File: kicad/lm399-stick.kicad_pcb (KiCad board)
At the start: 4 copper layers, 48.3 x 48.3 mm, 14 parts, among them P1 CONN_5X1, U1 LM399A, U2 OP07

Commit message: v1
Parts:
- removed the G*** at (59.7, 54.0)
- removed the H*** at (167.6, 133.3)
- removed the H*** at (208.3, 133.3)
- removed the H*** at (208.3, 174.0)
- removed the H*** at (167.6, 174.0)
- added C4: 10nF, ANYSSCAP_SMALL_2_059B_0805, F.Cu at (165.1, 143.5)
- added G***: OSHW-logo_silkscreen-front_3mm, OSHW-logo_silkscreen-front_3mm, F.Cu at (196.2, 139.1)
- added H***: VAL**, SIL-1, F.Cu at (209.6, 137.2)
- added H***: VAL**, SIL-1, F.Cu at (209.6, 149.9)
- added P2: CONN_1X1, SIL-1, F.Cu at (165.1, 137.2)
- added P3: CONN_1X1, SIL-1, F.Cu at (188.0, 144.8)
- added P4: CONN_1X1, SIL-1, F.Cu at (188.0, 142.2)
- added P5: CONN_2X1, SIL-2, F.Cu at (182.9, 149.9)
- added R4: 200k, R_AXIAL_0W25_059A_PL, F.Cu at (185.4, 147.3)
- C1, C2, C3: footprint CERCAP_2_059A -> ANYSSCAP_SMALL_2_059B_0805
- P1: value CONN_5X1 -> CONN_1X1; footprint 4455-N2-5 -> SIL-1
- moved U1 28.4 mm to (203.8, 141.6), turned to 0 degrees
- moved P1 26.8 mm to (165.1, 149.9)
- moved R1 15.7 mm to (182.9, 137.2)
- moved C1 10.6 mm to (191.1, 143.5)
- moved R2 10.5 mm to (167.6, 138.4)
- moved U2 6.35 mm to (180.3, 144.8), turned to 90 degrees
- moved R3 5.68 mm to (170.2, 148.6)
- moved C2 5.39 mm to (191.8, 149.9), turned to 0 degrees
- moved C3 5.39 mm to (176.5, 149.9), turned to 0 degrees
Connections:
- C1 pad 1: +Vref -> +Vz
- C1 pad 2: -Vref -> -Vz
- C2 pad 1: 15V -> N-000002
- C2 pad 2: -Vref -> -Vz
- C3 pad 1: N-000006 -> Vcc
- C3 pad 2: N-000007 -> -Vz
- P1 pad 1: 15V -> Vcc
- R1 pad 1: N-000006 -> N-000004
- R1 pad 2: +Vref -> +Vz
- R2 pad 1: N-000006 -> N-000004
- R3 pad 2: -Vref -> -Vz
- U1 pad 1: +Vref -> +Vz
- U1 pad 2: -Vref -> -Vz
- U1 pad 3: 15V -> N-000002
- U1 pad 4: -Vref -> -Vz
- U2 pad 3: +Vref -> +Vz
- U2 pad 4: -Vref -> -Vz
- U2 pad 6: N-000006 -> N-000004
- U2 pad 7: 15V -> Vcc
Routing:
- net -Vref: track 160.4 -> 0.00 mm
- net -Vz: track 0.00 -> 131.7 mm
- net 15V: track 77.4 -> 0.00 mm
- net +Vref: track 70.2 -> 0.00 mm
- net +Vz: track 0.00 -> 63.8 mm
- net Vcc: track 0.00 -> 31.1 mm
- net N-000006: track 25.0 -> 0.00 mm
- net N-000002: track 0.00 -> 23.7 mm
- net N-000004: track 0.00 -> 20.4 mm
- net N-000007: track 15.5 -> 23.7 mm
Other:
- board size 48.3 x 48.3 mm -> 48.3 x 16.5 mm
- board text added: "+Vz"
- board text added: "-Vz"
- board text added: "GND"
- board text added: "LM399 on a stick!"
- board text added: "VCC"
- board text added: "github.com/pepaslabs/lm399-stick"
- board text removed: "Small LM399"
- board text removed: "github.com/pepaslabs/small-lm399"

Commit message: correcting cap values
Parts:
- C3: value 10nF -> 0.1uF
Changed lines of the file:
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@@
     (links 25)
     (no_connects 0)
-    (area 145.999999 116.789999 237.540001 190.550001)
+    (area 161.383134 133.9088 211.996866 153.1112)
     (thickness 1.6)
     (drawings 31)
@@
       (effects (font (size 0.635 0.635) (thickness 0.127)))
     )
-    (fp_text value 10nF (at 2.54 -1.905) (layer F.SilkS)
-      (effects (font (size 0.635 0.635) (thickness 0.127)))
-    )
+    (fp_text value 0.1uF (at 2.54 -1.905) (layer F.SilkS)
+      (effects (font (size 0.635 0.635) (thickness 0.127)))
+    )

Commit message: v1.1
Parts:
- removed the H*** at (209.6, 137.2)
- removed the H*** at (209.6, 149.9)
- added H***: Val**, 1pin_056_079, F.Cu at (209.6, 149.9)
- added H***: Val**, 1pin_056_079, F.Cu at (209.6, 137.2)
- P1, P2, P3, P4: footprint SIL-1 -> 1pin_056_079
- moved P4 0.64 mm to (188.0, 141.6)
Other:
- board text added: "v1.1"
- board text removed: "v1"
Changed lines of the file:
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@@
     (links 25)
     (no_connects 0)
-    (area 161.383134 133.9088 211.996866 153.1112)
+    (area 163.144999 135.204999 211.505001 151.815001)
     (thickness 1.6)
     (drawings 31)
@@
     (mod_text_size 1 1)
     (mod_text_width 0.15)
-    (pad_size 0.8128 0.8128)
-    (pad_drill 0.4064)
+    (pad_size 2.0066 2.0066)
+    (pad_drill 1.4224)
     (pad_to_mask_clearance 0)
     (aux_axis_origin 0 0)
@@
     )
   )
-  (module SIL-1 (layer F.Cu)
-    (at 165.1 149.86)
-    (descr "Connecteurs 1 pin")
-    (tags "CONN DEV")
-    (fp_text reference P1 (at 0 2.54) (layer F.SilkS) hide
-      (effects (font (size 0.762 0.762) (thickness 0.1524)))
-    )
-    (fp_text value CONN_1X1 (at 0 -2.54) (layer F.SilkS) hide
-      (effects (font (size 0.762 0.762) (thickness 0.1524)))
-    )
-    (fp_line (start -1.27 1.27) (end 1.27 1.27) (layer F.SilkS) (width 0.254))
-    (fp_line (start -1.27 -1.27) (end 1.27 -1.27) (layer F.SilkS) (width 0.254))
-    (fp_line (start -1.27 1.27) (end -1.27 -1.27) (layer F.SilkS) (width 0.254))
-    (fp_line (start 1.27 -1.27) (end 1.27 1.27) (layer F.SilkS) (width 0.254))
-    (pad 1 thru_hole rect (at 0 0) (size 1.7526 1.7526) (drill 1.016)
-      (layers *.Cu *.Mask F.SilkS)
-      (net 6 Vcc)
-    )
-  )
-  (module SIL-1 (layer F.Cu)
-    (at 165.1 137.16)
-    (descr "Connecteurs 1 pin")
-    (tags "CONN DEV")
-    (fp_text reference P2 (at 0 2.54) (layer F.SilkS) hide
-      (effects (font (size 0.762 0.762) (thickness 0.1524)))
-    )
-    (fp_text value CONN_1X1 (at 0 -2.54) (layer F.SilkS) hide
-      (effects (font (size 0.762 0.762) (thickness 0.1524)))
-    )
-    (fp_line (start -1.27 1.27) (end 1.27 1.27) (layer F.SilkS) (width 0.254))
-    (fp_line (start -1.27 -1.27) (end 1.27 -1.27) (layer F.SilkS) (width 0.254))
-    (fp_line (start -1.27 1.27) (end -1.27 -1.27) (layer F.SilkS) (width 0.254))
-    (fp_line (start 1.27 -1.27) (end 1.27 1.27) (layer F.SilkS) (width 0.254))
-    (pad 1 thru_hole rect (at 0 0) (size 1.7526 1.7526) (drill 1.016)
-      (layers *.Cu *.Mask F.SilkS)
-      (net 2 -Vz)
-    )
-  )
-  (module SIL-1 (layer F.Cu)
-    (at 187.96 144.78)
-    (descr "Connecteurs 1 pin")
-    (tags "CONN DEV")
-    (fp_text reference P3 (at 0 2.54) (layer F.SilkS) hide
-      (effects (font (size 0.762 0.762) (thickness 0.1524)))
-    )
-    (fp_text value CONN_1X1 (at 0 -2.54) (layer F.SilkS) hide
-      (effects (font (size 0.762 0.762) (thickness 0.1524)))
-    )
-    (fp_line (start -1.27 1.27) (end 1.27 1.27) (layer F.SilkS) (width 0.254))
-    (fp_line (start -1.27 -1.27) (end 1.27 -1.27) (layer F.SilkS) (width 0.254))
-    (fp_line (start -1.27 1.27) (end -1.27 -1.27) (layer F.SilkS) (width 0.254))
-    (fp_line (start 1.27 -1.27) (end 1.27 1.27) (layer F.SilkS) (width 0.254))
-    (pad 1 thru_hole rect (at 0 0) (size 1.7526 1.7526) (drill 1.016)
-      (layers *.Cu *.Mask F.SilkS)
-      (net 1 +Vz)
-    )
-  )
-  (module SIL-1 (layer F.Cu)
-    (at 187.96 142.24)
-    (descr "Connecteurs 1 pin")
-    (tags "CONN DEV")
-    (fp_text reference P4 (at 0 2.54) (layer F.SilkS) hide
-      (effects (font (size 0.762 0.762) (thickness 0.1524)))
-    )
-    (fp_text value CONN_1X1 (at 0 -2.54) (layer F.SilkS) hide
-      (effects (font (size 0.762 0.762) (thickness 0.1524)))
-    )
-    (fp_line (start -1.27 1.27) (end 1.27 1.27) (layer F.SilkS) (width 0.254))
-    (fp_line (start -1.27 -1.27) (end 1.27 -1.27) (layer F.SilkS) (width 0.254))
-    (fp_line (start -1.27 1.27) (end -1.27 -1.27) (layer F.SilkS) (width 0.254))
-    (fp_line (start 1.27 -1.27) (end 1.27 1.27) (layer F.SilkS) (width 0.254))
-    (pad 1 thru_hole rect (at 0 0) (size 1.7526 1.7526) (drill 1.016)
-      (layers *.Cu *.Mask F.SilkS)
-      (net 2 -Vz)
-    )
-  )
   (module R_AXIAL_0W25_059A_PL (layer F.Cu)
     (at 167.64 138.43 270)
@@
       (layers *.Cu *.Mask F.SilkS)
       (net 3 N-000002)
-    )
-  )
-  (module SIL-1 (layer F.Cu)
-    (at 209.55 137.16)
-    (descr "Connecteurs 1 pin")
-    (tags "CONN DEV")
-    (fp_text reference H*** (at 0 2.54) (layer F.SilkS) hide
-      (effects (font (size 0.762 0.762) (thickness 0.1524)))
-    )
-    (fp_text value VAL** (at 0 -2.54) (layer F.SilkS) hide
-      (effects (font (size 0.762 0.762) (thickness 0.1524)))
-    )
-    (fp_line (start -1.27 1.27) (end 1.27 1.27) (layer F.SilkS) (width 0.254))
-    (fp_line (start -1.27 -1.27) (end 1.27 -1.27) (layer F.SilkS) (width 0.254))
-    (fp_line (start -1.27 1.27) (end -1.27 -1.27) (layer F.SilkS) (width 0.254))
-    (fp_line (start 1.27 -1.27) (end 1.27 1.27) (layer F.SilkS) (width 0.254))
-    (pad 1 thru_hole rect (at 0 0) (size 1.7526 1.7526) (drill 1.016)
-      (layers *.Cu *.Mask F.SilkS)
-    )
-  )
-  (module SIL-1 (layer F.Cu)
-    (at 209.55 149.86)
-    (descr "Connecteurs 1 pin")
-    (tags "CONN DEV")
-    (fp_text reference H*** (at 0 2.54) (layer F.SilkS) hide
-      (effects (font (size 0.762 0.762) (thickness 0.1524)))
-    )
-    (fp_text value VAL** (at 0 -2.54) (layer F.SilkS) hide
-      (effects (font (size 0.762 0.762) (thickness 0.1524)))
-    )
-    (fp_line (start -1.27 1.27) (end 1.27 1.27) (layer F.SilkS) (width 0.254))
-    (fp_line (start -1.27 -1.27) (end 1.27 -1.27) (layer F.SilkS) (width 0.254))
-    (fp_line (start -1.27 1.27) (end -1.27 -1.27) (layer F.SilkS) (width 0.254))
-    (fp_line (start 1.27 -1.27) (end 1.27 1.27) (layer F.SilkS) (width 0.254))
-    (pad 1 thru_hole rect (at 0 0) (size 1.7526 1.7526) (drill 1.016)
-      (layers *.Cu *.Mask F.SilkS)
     )
   )
@@
       (xy -0.90932 1.3462)) (layer F.SilkS) (width 0.00254))
   )
+  (module 1pin_056_079 (layer F.Cu)
+    (at 165.1 137.16)
+    (descr "1 pin, 0.056\" drill, 0.079\" round pad")
+    (fp_text reference P2 (at 0 -2.54) (layer F.SilkS) hide
+      (effects (font (size 1.016 1.016) (thickness 0.254)))
+    )
+    (fp_text value CONN_1X1 (at 0 2.54) (layer F.SilkS) hide
+      (effects (font (size 1.016 1.016) (thickness 0.254)))
+    )
+    (pad 1 thru_hole circle (at 0 0) (size 2.0066 2.0066) (drill 1.4224)
+      (layers *.Cu *.Mask F.SilkS)
+      (net 2 -Vz)
+    )
+  )
+  (module 1pin_056_079 (layer F.Cu)
+    (at 165.1 149.86)
+    (descr "1 pin, 0.056\" drill, 0.079\" round pad")
+    (fp_text reference P1 (at 0 -2.54) (layer F.SilkS) hide
+      (effects (font (size 1.016 1.016) (thickness 0.254)))
+    )
+    (fp_text value CONN_1X1 (at 0 2.54) (layer F.SilkS) hide
+      (effects (font (size 1.016 1.016) (thickness 0.254)))
+    )
+    (pad 1 thru_hole rect (at 0 0) (size 2.0066 2.0066) (drill 1.4224)
+      (layers *.Cu *.Mask F.SilkS)
+      (net 6 Vcc)
+    )
+  )
+  (module 1pin_056_079 (layer F.Cu)
+    (at 209.55 149.86)
+    (descr "1 pin, 0.056\" drill, 0.079\" round pad")
+    (path 1pin)
+    (fp_text reference H*** (at 0 -2.54) (layer F.SilkS) hide
+      (effects (font (size 1.016 1.016) (thickness 0.254)))
+    )
+    (fp_text value Val** (at 0 2.54) (layer F.SilkS) hide
+      (effects (font (size 1.016 1.016) (thickness 0.254)))
+    )
+    (pad 1 thru_hole circle (at 0 0) (size 2.0066 2.0066) (drill 1.4224)
+      (layers *.Cu *.Mask F.SilkS)
+    )
+  )
+  (module 1pin_056_079 (layer F.Cu)
+    (at 209.55 137.16)
+    (descr "1 pin, 0.056\" drill, 0.079\" round pad")
+    (path 1pin)
+    (fp_text reference H*** (at 0 -2.54) (layer F.SilkS) hide
+      (effects (font (size 1.016 1.016) (thickness 0.254)))
+    )
+    (fp_text value Val** (at 0 2.54) (layer F.SilkS) hide
+      (effects (font (size 1.016 1.016) (thickness 0.254)))
+    )
+    (pad 1 thru_hole circle (at 0 0) (size 2.0066 2.0066) (drill 1.4224)
+      (layers *.Cu *.Mask F.SilkS)
+    )
+  )
+  (module 1pin_056_079 (layer F.Cu)
+    (at 187.96 141.605)
+    (descr "1 pin, 0.056\" drill, 0.079\" round pad")
+    (fp_text reference P4 (at 0 -2.54) (layer F.SilkS) hide
+      (effects (font (size 1.016 1.016) (thickness 0.254)))
+    )
+    (fp_text value CONN_1X1 (at 0 2.54) (layer F.SilkS) hide
+      (effects (font (size 1.016 1.016) (thickness 0.254)))
+    )
+    (pad 1 thru_hole circle (at 0 0) (size 2.0066 2.0066) (drill 1.4224)
+      (layers *.Cu *.Mask F.SilkS)
+      (net 2 -Vz)
+    )
+  )
+  (module 1pin_056_079 (layer F.Cu)
+    (at 187.96 144.78)
+    (descr "1 pin, 0.056\" drill, 0.079\" round pad")
+    (fp_text reference P3 (at 0 -2.54) (layer F.SilkS) hide
+      (effects (font (size 1.016 1.016) (thickness 0.254)))
+    )
+    (fp_text value CONN_1X1 (at 0 2.54) (layer F.SilkS) hide
+      (effects (font (size 1.016 1.016) (thickness 0.254)))
+    )
+    (pad 1 thru_hole rect (at 0 0) (size 2.0066 2.0066) (drill 1.4224)
+      (layers *.Cu *.Mask F.SilkS)
+      (net 1 +Vz)
+    )
+  )
   (gr_text +Vz (at 186.69 147.32) (layer F.SilkS)
     (effects (font (size 0.762 0.762) (thickness 0.1524)) (justify left))
@@
   (gr_arc (start 163.83 135.89) (end 163.195 135.89) (angle 90) (layer Edge.Cuts) (width 0.1))
   (gr_arc (start 163.83 151.13) (end 163.83 151.765) (angle 90) (layer Edge.Cuts) (width 0.1))
-  (gr_text v1 (at 199.39 136.525) (layer F.SilkS)
+  (gr_text v1.1 (at 199.39 136.525) (layer F.SilkS)
     (effects (font (size 0.635 0.635) (thickness 0.127)))
   )
@@
       )
     )
+  )
+  (zone (net 0) (net_name "") (layer B.SilkS) (hatch edge 0.508)
+    (connect_pads (clearance 0.508))
+    (min_thickness 0.254)
+    (fill (arc_segments 16) (thermal_gap 0.508) (thermal_bridge_width 0.508))
+    (polygon
+      (pts
+        (xy 179.07 148.59) (xy 173.99 148.59) (xy 173.99 135.89) (xy 179.07 135.89)
+      )
+    )

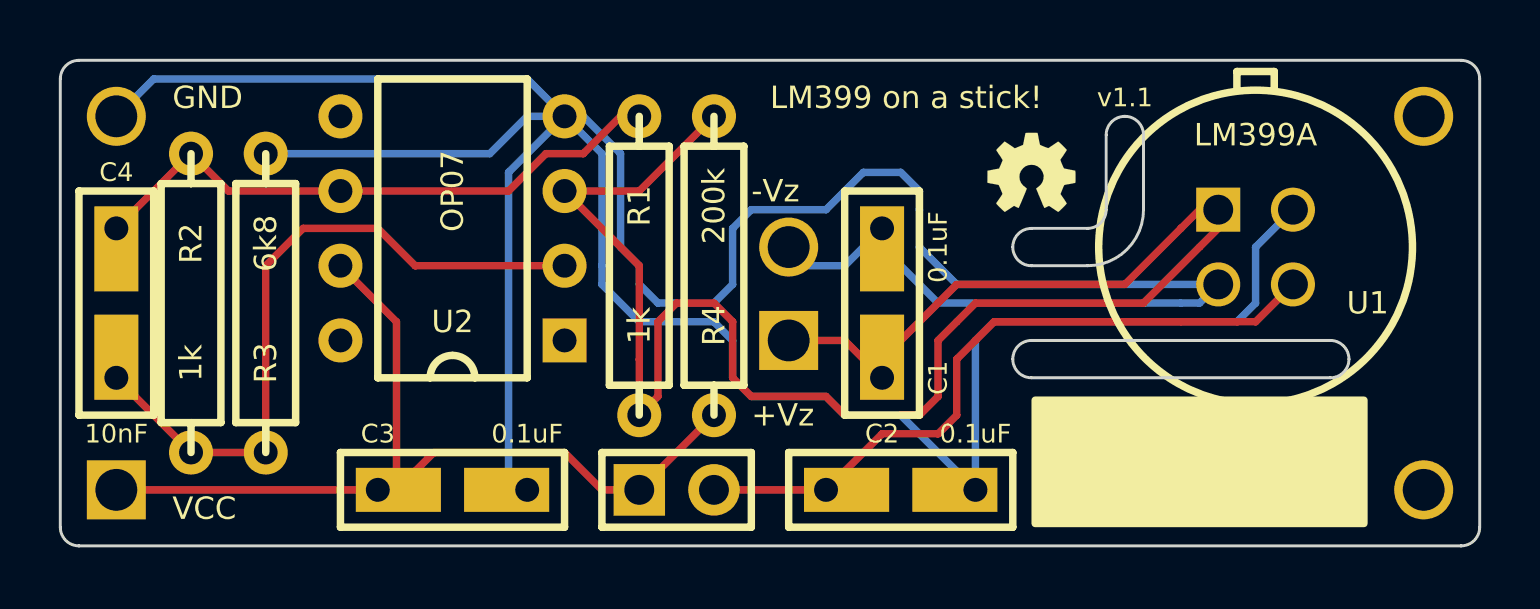
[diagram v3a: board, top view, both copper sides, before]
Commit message: using machine pin header footprints
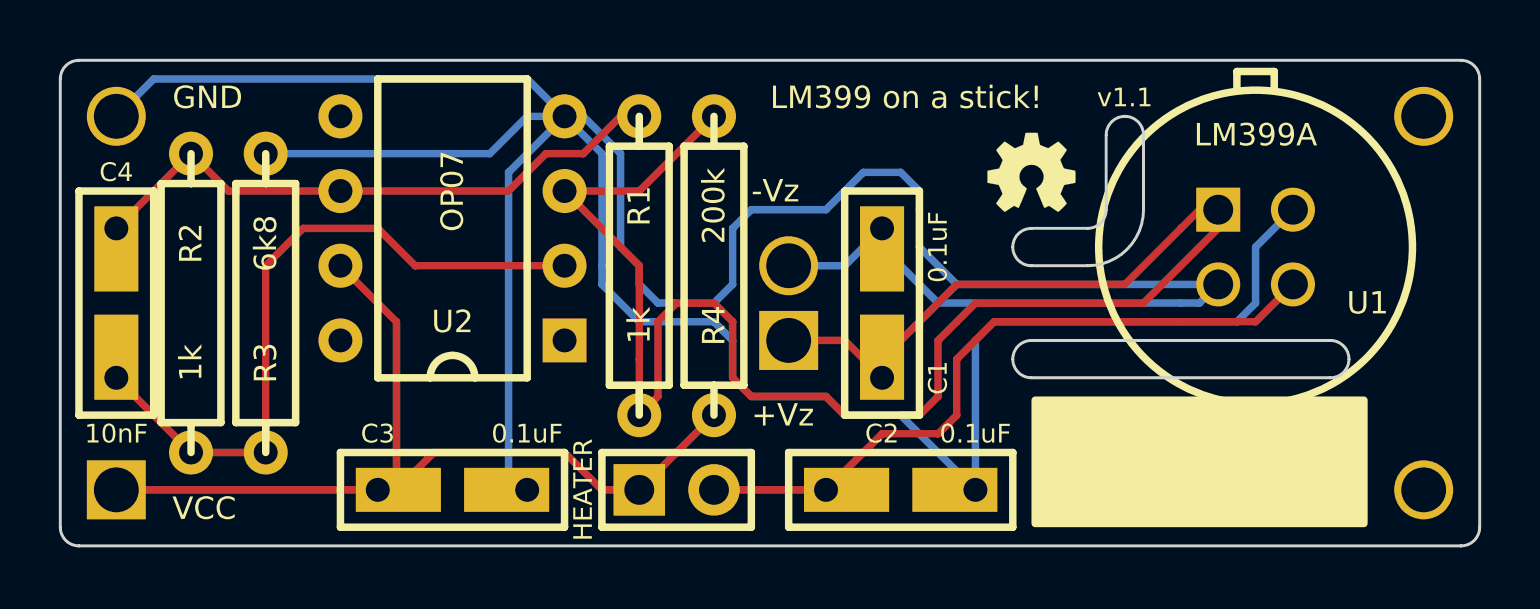
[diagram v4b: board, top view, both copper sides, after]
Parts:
- removed the H*** at (209.6, 149.9)
- removed the H*** at (209.6, 137.2)
- added H***: Val**, 1pin_060_079, F.Cu at (209.6, 137.2)
- added H***: Val**, 1pin_060_079, F.Cu at (209.6, 149.9)
- P1, P2, P3, P4: footprint 1pin_056_079 -> 1pin_060_079
- moved P4 0.64 mm to (188.0, 142.2)
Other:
- board text added: "HEATER"
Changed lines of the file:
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@@
     (links 25)
     (no_connects 0)
-    (area 163.144999 135.204999 211.505001 151.815001)
+    (area 160.203445 133.731 212.753222 153.289)
     (thickness 1.6)
-    (drawings 31)
+    (drawings 32)
     (tracks 124)
     (zones 0)
@@
     (mod_text_width 0.15)
     (pad_size 2.0066 2.0066)
-    (pad_drill 1.4224)
+    (pad_drill 1.524)
     (pad_to_mask_clearance 0)
     (aux_axis_origin 0 0)
@@
       (xy -0.90932 1.3462)) (layer F.SilkS) (width 0.00254))
   )
-  (module 1pin_056_079 (layer F.Cu)
-    (at 165.1 137.16)
-    (descr "1 pin, 0.056\" drill, 0.079\" round pad")
-    (fp_text reference P2 (at 0 -2.54) (layer F.SilkS) hide
-      (effects (font (size 1.016 1.016) (thickness 0.254)))
-    )
-    (fp_text value CONN_1X1 (at 0 2.54) (layer F.SilkS) hide
-      (effects (font (size 1.016 1.016) (thickness 0.254)))
-    )
-    (pad 1 thru_hole circle (at 0 0) (size 2.0066 2.0066) (drill 1.4224)
-      (layers *.Cu *.Mask F.SilkS)
-      (net 2 -Vz)
-    )
-  )
-  (module 1pin_056_079 (layer F.Cu)
-    (at 165.1 149.86)
-    (descr "1 pin, 0.056\" drill, 0.079\" round pad")
-    (fp_text reference P1 (at 0 -2.54) (layer F.SilkS) hide
-      (effects (font (size 1.016 1.016) (thickness 0.254)))
-    )
-    (fp_text value CONN_1X1 (at 0 2.54) (layer F.SilkS) hide
-      (effects (font (size 1.016 1.016) (thickness 0.254)))
-    )
-    (pad 1 thru_hole rect (at 0 0) (size 2.0066 2.0066) (drill 1.4224)
-      (layers *.Cu *.Mask F.SilkS)
-      (net 6 Vcc)
-    )
-  )
-  (module 1pin_056_079 (layer F.Cu)
-    (at 209.55 149.86)
-    (descr "1 pin, 0.056\" drill, 0.079\" round pad")
+  (module 1pin_060_079 (layer F.Cu)
+    (at 209.55 137.16)
+    (descr "1 pin, 0.060\" drill, 0.079\" round pad")
     (path 1pin)
     (fp_text reference H*** (at 0 -2.54) (layer F.SilkS) hide
@@
       (effects (font (size 1.016 1.016) (thickness 0.254)))
     )
-    (pad 1 thru_hole circle (at 0 0) (size 2.0066 2.0066) (drill 1.4224)
-      (layers *.Cu *.Mask F.SilkS)
-    )
-  )
-  (module 1pin_056_079 (layer F.Cu)
-    (at 209.55 137.16)
-    (descr "1 pin, 0.056\" drill, 0.079\" round pad")
+    (pad 1 thru_hole circle (at 0 0) (size 2.0066 2.0066) (drill 1.524)
+      (layers *.Cu *.Mask F.SilkS)
+    )
+  )
+  (module 1pin_060_079 (layer F.Cu)
+    (at 209.55 149.86)
+    (descr "1 pin, 0.060\" drill, 0.079\" round pad")
     (path 1pin)
     (fp_text reference H*** (at 0 -2.54) (layer F.SilkS) hide
@@
       (effects (font (size 1.016 1.016) (thickness 0.254)))
     )
-    (pad 1 thru_hole circle (at 0 0) (size 2.0066 2.0066) (drill 1.4224)
-      (layers *.Cu *.Mask F.SilkS)
-    )
-  )
-  (module 1pin_056_079 (layer F.Cu)
-    (at 187.96 141.605)
-    (descr "1 pin, 0.056\" drill, 0.079\" round pad")
+    (pad 1 thru_hole circle (at 0 0) (size 2.0066 2.0066) (drill 1.524)
+      (layers *.Cu *.Mask F.SilkS)
+    )
+  )
+  (module 1pin_060_079 (layer F.Cu)
+    (at 165.1 149.86)
+    (descr "1 pin, 0.060\" drill, 0.079\" round pad")
+    (fp_text reference P1 (at 0 -2.54) (layer F.SilkS) hide
+      (effects (font (size 1.016 1.016) (thickness 0.254)))
+    )
+    (fp_text value CONN_1X1 (at 0 2.54) (layer F.SilkS) hide
+      (effects (font (size 1.016 1.016) (thickness 0.254)))
+    )
+    (pad 1 thru_hole rect (at 0 0) (size 2.0066 2.0066) (drill 1.524)
+      (layers *.Cu *.Mask F.SilkS)
+      (net 6 Vcc)
+    )
+  )
+  (module 1pin_060_079 (layer F.Cu)
+    (at 165.1 137.16)
+    (descr "1 pin, 0.060\" drill, 0.079\" round pad")
+    (fp_text reference P2 (at 0 -2.54) (layer F.SilkS) hide
+      (effects (font (size 1.016 1.016) (thickness 0.254)))
+    )
+    (fp_text value CONN_1X1 (at 0 2.54) (layer F.SilkS) hide
+      (effects (font (size 1.016 1.016) (thickness 0.254)))
+    )
+    (pad 1 thru_hole circle (at 0 0) (size 2.0066 2.0066) (drill 1.524)
+      (layers *.Cu *.Mask F.SilkS)
+      (net 2 -Vz)
+    )
+  )
+  (module 1pin_060_079 (layer F.Cu)
+    (at 187.96 142.24)
+    (descr "1 pin, 0.060\" drill, 0.079\" round pad")
     (fp_text reference P4 (at 0 -2.54) (layer F.SilkS) hide
       (effects (font (size 1.016 1.016) (thickness 0.254)))
@@
       (effects (font (size 1.016 1.016) (thickness 0.254)))
     )
-    (pad 1 thru_hole circle (at 0 0) (size 2.0066 2.0066) (drill 1.4224)
-      (layers *.Cu *.Mask F.SilkS)
-      (net 2 -Vz)
-    )
-  )
-  (module 1pin_056_079 (layer F.Cu)
+    (pad 1 thru_hole circle (at 0 0) (size 2.0066 2.0066) (drill 1.524)
+      (layers *.Cu *.Mask F.SilkS)
+      (net 2 -Vz)
+    )
+  )
+  (module 1pin_060_079 (layer F.Cu)
     (at 187.96 144.78)
-    (descr "1 pin, 0.056\" drill, 0.079\" round pad")
+    (descr "1 pin, 0.060\" drill, 0.079\" round pad")
     (fp_text reference P3 (at 0 -2.54) (layer F.SilkS) hide
       (effects (font (size 1.016 1.016) (thickness 0.254)))
@@
       (effects (font (size 1.016 1.016) (thickness 0.254)))
     )
-    (pad 1 thru_hole rect (at 0 0) (size 2.0066 2.0066) (drill 1.4224)
+    (pad 1 thru_hole rect (at 0 0) (size 2.0066 2.0066) (drill 1.524)
       (layers *.Cu *.Mask F.SilkS)
       (net 1 +Vz)
     )
   )
+  (gr_text HEATER (at 180.975 149.86 90) (layer F.SilkS)
+    (effects (font (size 0.635 0.635) (thickness 0.127)))
+  )
   (gr_text +Vz (at 186.69 147.32) (layer F.SilkS)
